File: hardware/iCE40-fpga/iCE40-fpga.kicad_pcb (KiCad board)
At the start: 4 copper layers, 50 x 22.9 mm, 64 parts, among them J1 USB_B_Micro, J2 JST_PH, J3 Feather, Q1 DMP2045U, U1 MCP73831-2-OT, U2 W25Q32JVZP, U3 AP2112K-3.3, U4 ICE40UP5K-SG48ITR, U5 NCV8114ASN120T1G, U6 93C46B, U7 FT2232H, X1 DSC6101CI1A

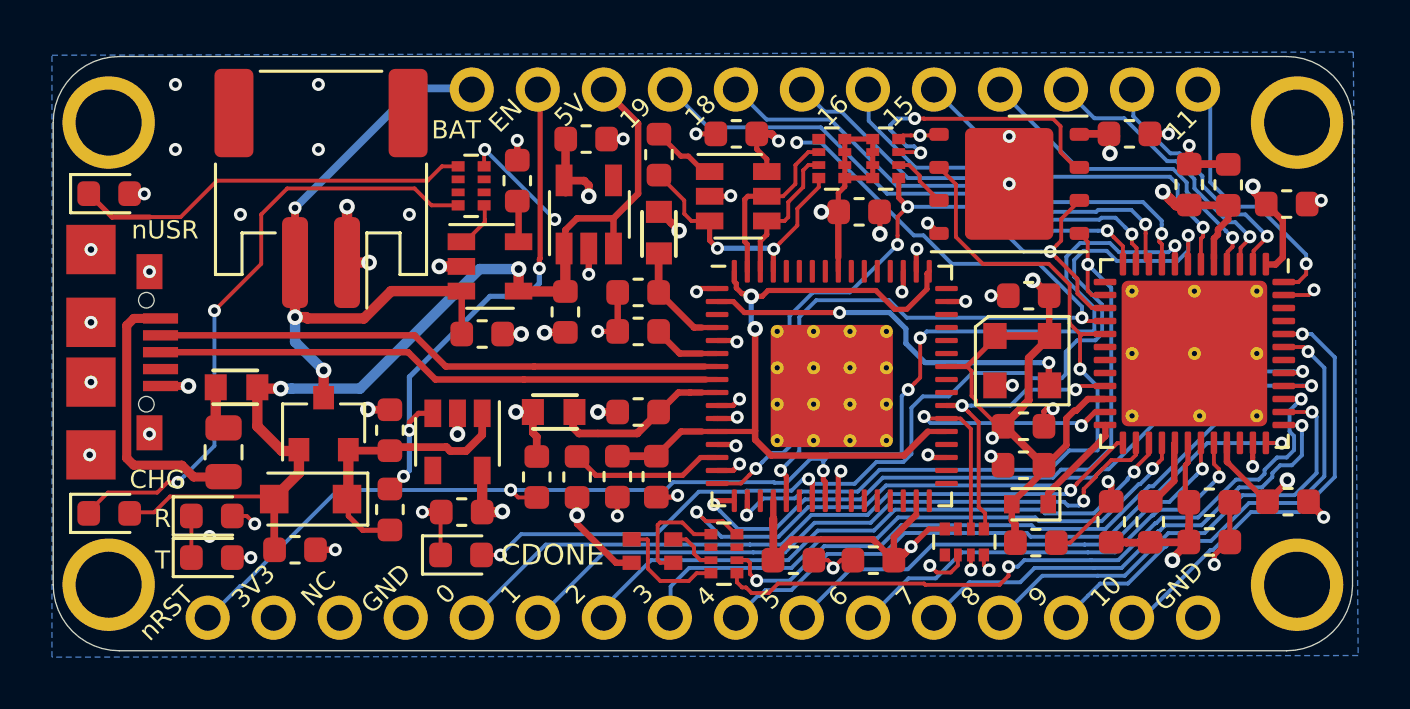
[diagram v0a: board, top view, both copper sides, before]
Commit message: broke out 4 pins to TP on bottom copper
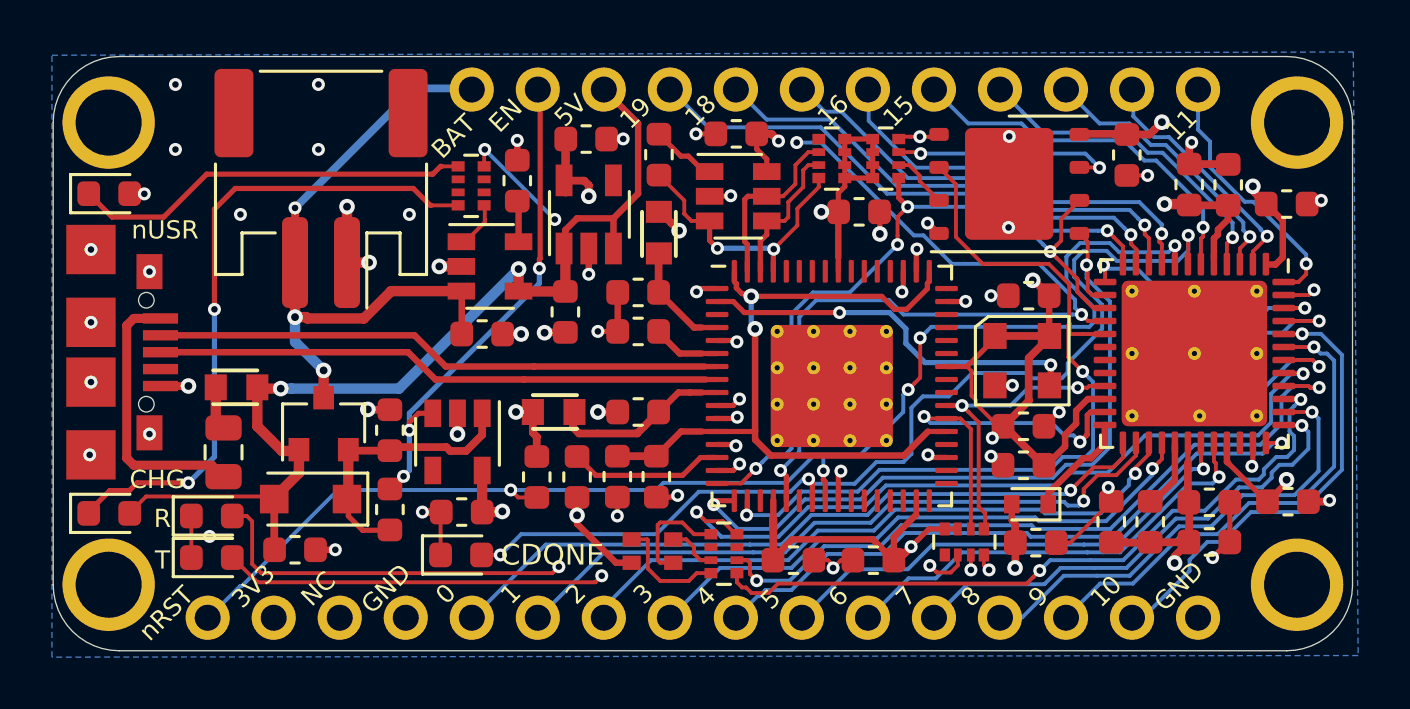
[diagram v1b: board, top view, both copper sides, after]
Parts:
- added TP1: 22, TestPoint:TestPoint_Pad_D1.5mm, B.Cu at (71.5, 35.1)
- added TP2: 20, TestPoint:TestPoint_Pad_D1.5mm, B.Cu at (71.5, 32.5)
- added TP3: 23, TestPoint:TestPoint_Pad_D1.5mm, B.Cu at (68.9, 35.1)
- added TP4: 21, TestPoint:TestPoint_Pad_D1.5mm, B.Cu at (68.9, 32.5)
- moved C7 0.82 mm to (67.6, 26.2), turned to 270 degrees
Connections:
- J1 pad 4: Net-(J1-Pad4) -> (no net)
- J3 pad 3: Net-(J3-Pad3) -> (no net)
- RN2 pad 1: Net-(RN2-Pad1) -> (no net)
- RN3 pad 3: Net-(RN3-Pad3) -> (no net)
- RN3 pad 6: Net-(RN3-Pad6) -> (no net)
- RN4 pad 1: Net-(RN4-Pad1) -> (no net)
- RN5 pad 2: Net-(RN5-Pad2) -> (no net)
- RN5 pad 3: Net-(RN5-Pad3) -> (no net)
- RN5 pad 6: Net-(RN5-Pad6) -> (no net)
- RN5 pad 7: Net-(RN5-Pad7) -> (no net)
- U3 pad 4: Net-(U3-Pad4) -> (no net)
- U4 pad 18: Net-(U4-Pad18) -> (no net)
- U4 pad 19: Net-(U4-Pad19) -> (no net)
- U4 pad 20: Net-(U4-Pad20) -> (no net)
- U4 pad 34: Net-(U4-Pad34) -> (no net)
- U5 pad 4: Net-(U5-Pad4) -> (no net)
- U7 pad 19: Net-(U7-Pad19) -> (no net)
- U7 pad 22: Net-(U7-Pad22) -> (no net)
- U7 pad 26: Net-(U7-Pad26) -> (no net)
- U7 pad 27: Net-(U7-Pad27) -> (no net)
- U7 pad 28: Net-(U7-Pad28) -> (no net)
- U7 pad 29: Net-(U7-Pad29) -> (no net)
- U7 pad 3: Net-(U7-Pad3) -> (no net)
- U7 pad 30: Net-(U7-Pad30) -> (no net)
- U7 pad 32: Net-(U7-Pad32) -> (no net)
- U7 pad 33: Net-(U7-Pad33) -> (no net)
- U7 pad 34: Net-(U7-Pad34) -> (no net)
- U7 pad 36: Net-(U7-Pad36) -> (no net)
- U7 pad 40: Net-(U7-Pad40) -> (no net)
- U7 pad 41: Net-(U7-Pad41) -> (no net)
- U7 pad 43: Net-(U7-Pad43) -> (no net)
- U7 pad 44: Net-(U7-Pad44) -> (no net)
- U7 pad 45: Net-(U7-Pad45) -> (no net)
- U7 pad 46: Net-(U7-Pad46) -> (no net)
- U7 pad 48: Net-(U7-Pad48) -> (no net)
- U7 pad 52: Net-(U7-Pad52) -> (no net)
- U7 pad 53: Net-(U7-Pad53) -> (no net)
- U7 pad 54: Net-(U7-Pad54) -> (no net)
- U7 pad 55: Net-(U7-Pad55) -> (no net)
- U7 pad 57: Net-(U7-Pad57) -> (no net)
- U7 pad 58: Net-(U7-Pad58) -> (no net)
- U7 pad 59: Net-(U7-Pad59) -> (no net)
- U7 pad 60: Net-(U7-Pad60) -> (no net)
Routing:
- net Net-(TP3-Pad1): track 0.00 -> 8.50 mm, vias 0 -> 1
- net Net-(TP1-Pad1): track 0.00 -> 5.53 mm, vias 0 -> 1
- net Net-(TP4-Pad1): track 0.00 -> 4.37 mm, vias 0 -> 1
- net Net-(TP2-Pad1): track 0.00 -> 4.00 mm, vias 0 -> 1
- net /FLASH_nHOLD|IO3: track 11.3 -> 8.89 mm
- net +3V3: track 76.0 -> 73.7 mm, vias 14 -> 15
- net Net-(D8-Pad2): track 30.1 -> 31.9 mm
- net Net-(D1-Pad1): track 23.9 -> 25.3 mm
- net /nLED_GREEN: track 27.0 -> 28.2 mm
- net /IO11: track 10.7 -> 11.7 mm
- net /RX_FPGA: track 13.2 -> 14.1 mm
- net +1V2: track 66.4 -> 65.4 mm
- net /LDO_EN: track 20.0 -> 19.2 mm
- net /nICE_CRESET: track 52.4 -> 51.6 mm
- net /IO10: track 17.0 -> 17.7 mm
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
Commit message: generated gerbers, changed pin labelling to match constraints file
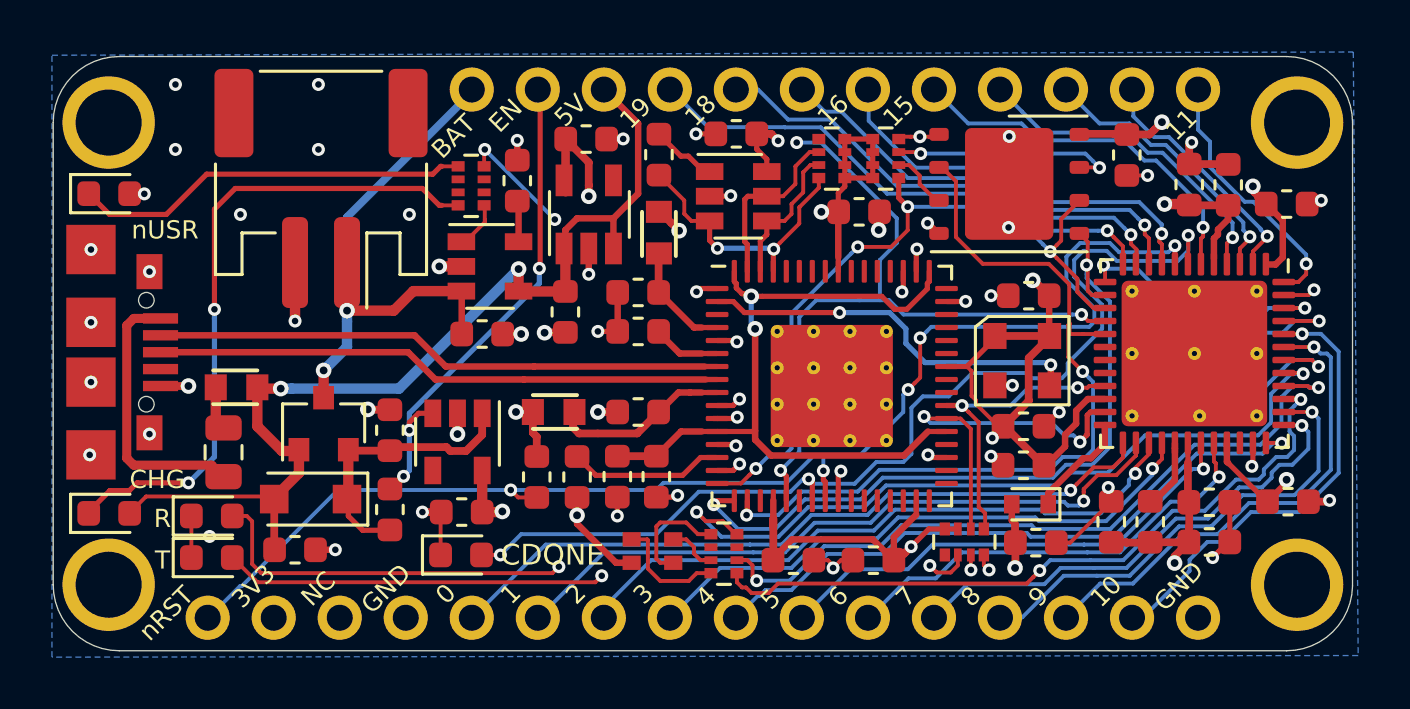
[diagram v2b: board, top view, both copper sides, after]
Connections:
- J2 pad 1: GND -> +BATT
- J2 pad 2: +BATT -> GND
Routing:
- net /ICE_SS: track 40.2 -> 34.8 mm
- net +BATT: track 25.0 -> 22.7 mm, vias 3 -> 2
- net +1V2: track 65.4 -> 66.6 mm
- net GND: track 49.5 -> 48.8 mm, vias 57 -> 56
- added copper zone on Layer3, net +3V3
- added copper zone on Layer2, net GND
- removed copper zone on 3V3, net +3V3
- removed copper zone on GND, net GND

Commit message: fixed LED footprint + power supply change to support battery
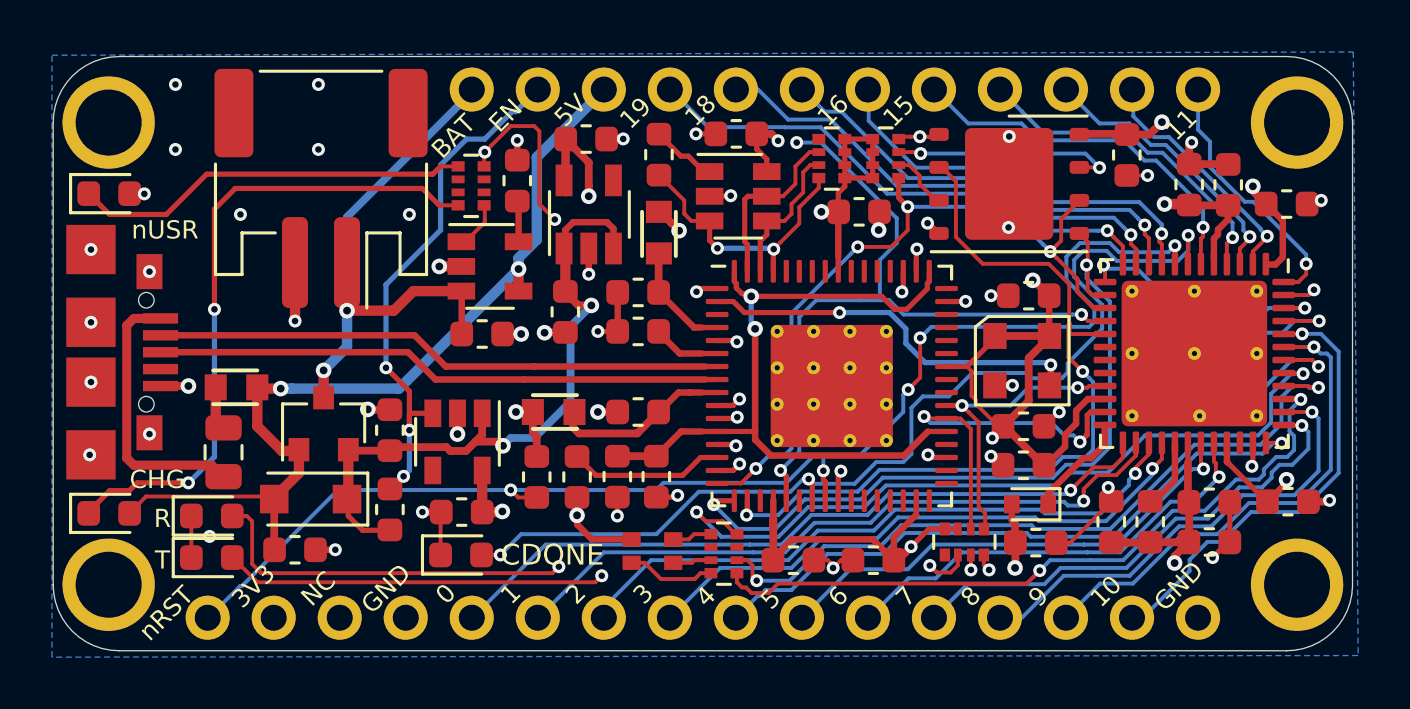
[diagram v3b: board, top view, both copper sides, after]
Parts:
- TP1: value 22 -> IO_22
- TP2: value 20 -> IO_20
- TP3: value 23 -> IO_23
- TP4: value 21 -> IO_21
- turned D6 to 270 degrees
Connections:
- net /IO0 renamed /IO_0
- net /IO1 renamed /IO_1
- net /IO10 renamed /IO_10
- net /IO11 renamed /IO_11
- net /IO12 renamed /IO_12
- net /IO13 renamed /IO_13
- net /IO14 renamed /IO_14
- net /IO15 renamed /IO_15
- net /IO16 renamed /IO_16
- net /IO17 renamed /IO_17
- net /IO18 renamed /IO_18
- net /IO19 renamed /IO_19
- net /IO2 renamed /IO_2
- net /IO3 renamed /IO_3
- net /IO4 renamed /IO_4
- net /IO5 renamed /IO_5
- net /IO6 renamed /IO_6
- net /IO7 renamed /IO_7
- net /IO8 renamed /IO_8
- net /IO9 renamed /IO_9
- net /RX_FPGA renamed /UART_RX
- net /TX_FPGA renamed /UART_TX
- net /nLED_BLUE renamed /nLED_BLU
- net /nLED_GREEN renamed /nLED_GRN
- C5 pad 1: +5V -> Net-(C1-Pad1)
- U5 pad 1: +5V -> Net-(C1-Pad1)
- U5 pad 3: +5V -> Net-(C1-Pad1)
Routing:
- net Net-(C1-Pad1): track 10.9 -> 25.5 mm, vias 0 -> 2
- net +5V: track 39.3 -> 34.6 mm
- net Net-(D6-Pad1): track 4.31 -> 1.53 mm
- net /nLED: track 39.6 -> 42.1 mm
- net /LDO_EN: track 19.2 -> 20.7 mm
- net Net-(D6-Pad3): track 4.48 -> 3.40 mm
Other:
- board text added: "12"
- board text added: "13"
- board text added: "14"
- board text added: "17"

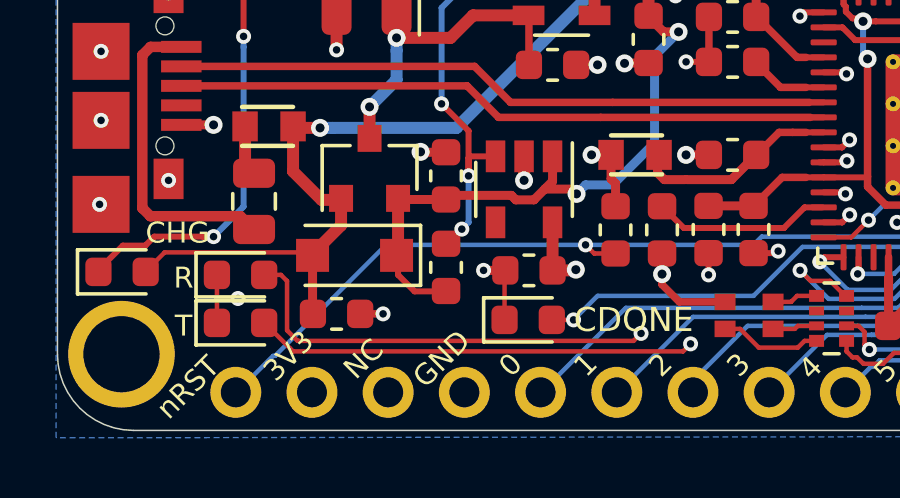
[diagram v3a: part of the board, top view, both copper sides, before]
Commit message: changed TX RX led direction
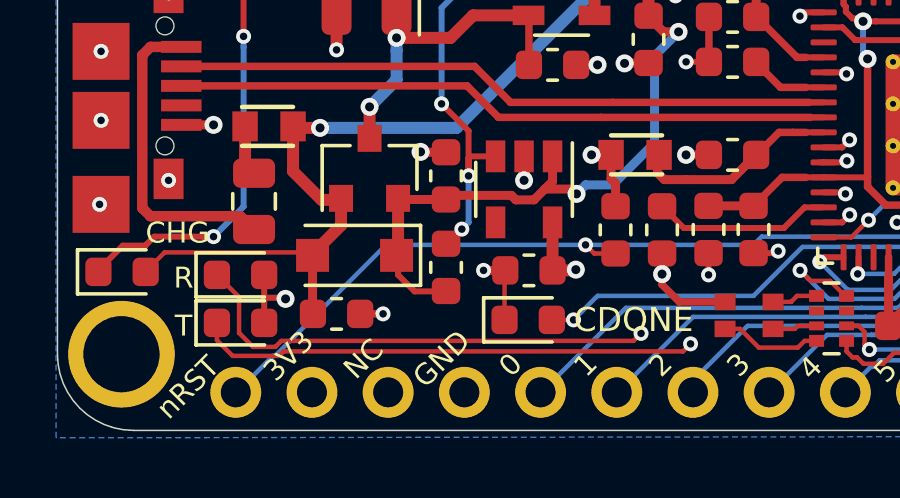
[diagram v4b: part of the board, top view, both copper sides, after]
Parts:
- D7: value LED -> RED
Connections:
- net /ICE_SCK renamed /FLASH_SCK
- net /ICE_SS renamed /FLASH_SS
- D3 pad 1: GND -> Net-(D3-Pad1)
- D3 pad 2: Net-(D3-Pad2) -> +3V3
- D8 pad 1: GND -> Net-(D8-Pad1)
- D8 pad 2: Net-(D8-Pad2) -> +3V3
- J1 pad 4: (no net) -> Net-(J1-Pad4)
- J3 pad 3: (no net) -> Net-(J3-Pad3)
- RN2 pad 1: (no net) -> Net-(RN2-Pad1)
- RN3 pad 3: (no net) -> Net-(RN3-Pad3)
- RN3 pad 6: (no net) -> Net-(RN3-Pad6)
- RN4 pad 1: (no net) -> Net-(RN4-Pad1)
- RN4 pad 3: Net-(D8-Pad2) -> Net-(D8-Pad1)
- RN4 pad 4: Net-(D3-Pad2) -> Net-(D3-Pad1)
- RN5 pad 2: (no net) -> Net-(RN5-Pad2)
- RN5 pad 3: (no net) -> Net-(RN5-Pad3)
- RN5 pad 6: (no net) -> Net-(RN5-Pad6)
- RN5 pad 7: (no net) -> Net-(RN5-Pad7)
- U3 pad 4: (no net) -> Net-(U3-Pad4)
- U4 pad 18: (no net) -> Net-(U4-Pad18)
- U4 pad 19: (no net) -> Net-(U4-Pad19)
- U4 pad 20: (no net) -> Net-(U4-Pad20)
- U4 pad 34: (no net) -> Net-(U4-Pad34)
- U5 pad 4: (no net) -> Net-(U5-Pad4)
- U7 pad 19: (no net) -> Net-(U7-Pad19)
- U7 pad 22: (no net) -> Net-(U7-Pad22)
- U7 pad 26: (no net) -> Net-(U7-Pad26)
- U7 pad 27: (no net) -> Net-(U7-Pad27)
- U7 pad 28: (no net) -> Net-(U7-Pad28)
- U7 pad 29: (no net) -> Net-(U7-Pad29)
- U7 pad 3: (no net) -> Net-(U7-Pad3)
- U7 pad 30: (no net) -> Net-(U7-Pad30)
- U7 pad 32: (no net) -> Net-(U7-Pad32)
- U7 pad 33: (no net) -> Net-(U7-Pad33)
- U7 pad 34: (no net) -> Net-(U7-Pad34)
- U7 pad 36: (no net) -> Net-(U7-Pad36)
- U7 pad 40: (no net) -> Net-(U7-Pad40)
- U7 pad 41: (no net) -> Net-(U7-Pad41)
- U7 pad 43: (no net) -> Net-(U7-Pad43)
- U7 pad 44: (no net) -> Net-(U7-Pad44)
- U7 pad 45: (no net) -> Net-(U7-Pad45)
- U7 pad 46: (no net) -> Net-(U7-Pad46)
- U7 pad 48: (no net) -> Net-(U7-Pad48)
- U7 pad 52: (no net) -> Net-(U7-Pad52)
- U7 pad 53: (no net) -> Net-(U7-Pad53)
- U7 pad 54: (no net) -> Net-(U7-Pad54)
- U7 pad 55: (no net) -> Net-(U7-Pad55)
- U7 pad 57: (no net) -> Net-(U7-Pad57)
- U7 pad 58: (no net) -> Net-(U7-Pad58)
- U7 pad 59: (no net) -> Net-(U7-Pad59)
- U7 pad 60: (no net) -> Net-(U7-Pad60)
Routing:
- net Net-(D3-Pad1): track 0.00 -> 33.4 mm, vias 0 -> 2
- net Net-(D8-Pad1): track 0.00 -> 33.4 mm, vias 0 -> 2
- net Net-(D8-Pad2): track 31.9 -> 0.00 mm, vias 2 -> 0
- net Net-(D3-Pad2): track 31.4 -> 0.00 mm, vias 2 -> 0
- net +3V3: track 73.3 -> 75.6 mm, vias 15 -> 16
- net GND: track 48.8 -> 46.5 mm, vias 56 -> 55

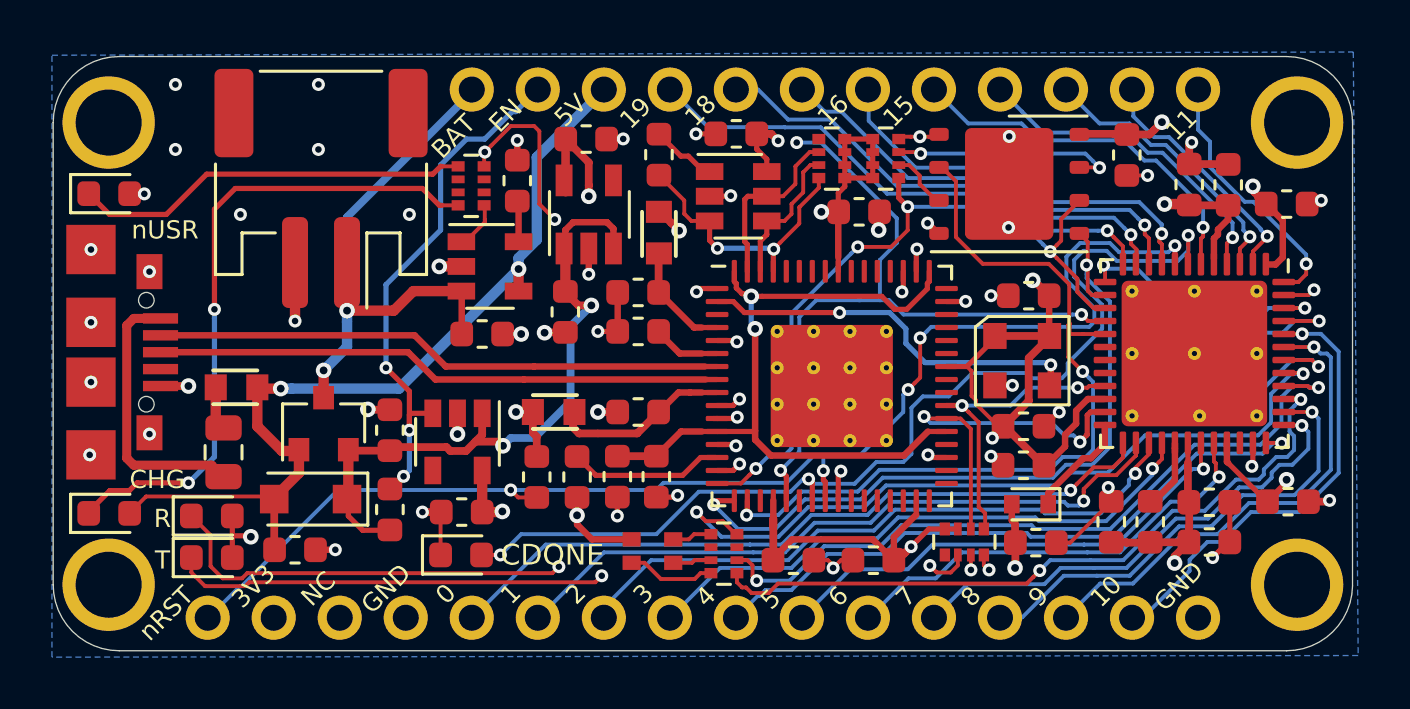
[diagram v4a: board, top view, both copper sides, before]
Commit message: updated feather footprint
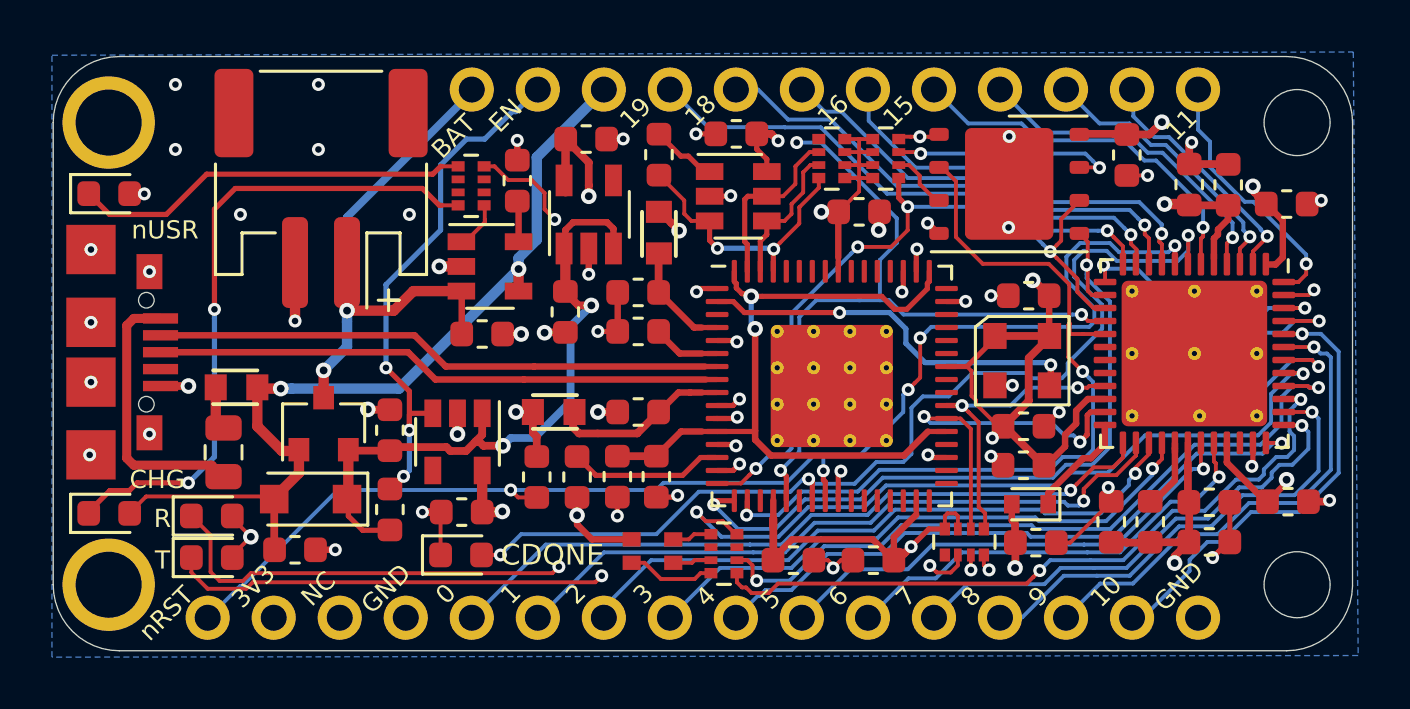
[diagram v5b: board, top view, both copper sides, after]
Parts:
- TP1: value IO_22 -> 22
- TP2: value IO_20 -> 20
- TP3: value IO_23 -> 23
- TP4: value IO_21 -> 21
- moved G*** 5.75 mm to (29.8, 35.7)
- moved REF** 4.74 mm to (41.0, 37.4)
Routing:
- net /nLED: track 42.1 -> 39.0 mm, vias 3 -> 2
- net +3V3: track 75.6 -> 77.6 mm
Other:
- board text added: "VUSB"
- board text removed: "5V"

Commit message: updated josh's details
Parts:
- added G***: LOGO, josh-logos:josh-johnson-logo-8_6x1_5, B.Cu at (41.6, 35.8)
